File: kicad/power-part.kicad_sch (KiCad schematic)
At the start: 53 parts, among them Q10 BSS84, Q11 BSS123N, Q12 ZXMP10A17GTA, Q2 IPT012N08N5, Q3 IPT012N08N5, Q4 IPT012N08N5, Q5 IPT012N08N5, Q6 IPT012N08N5, Q7 IPT012N08N5, Q8 IPT012N08N5, Q9 IPT012N08N5

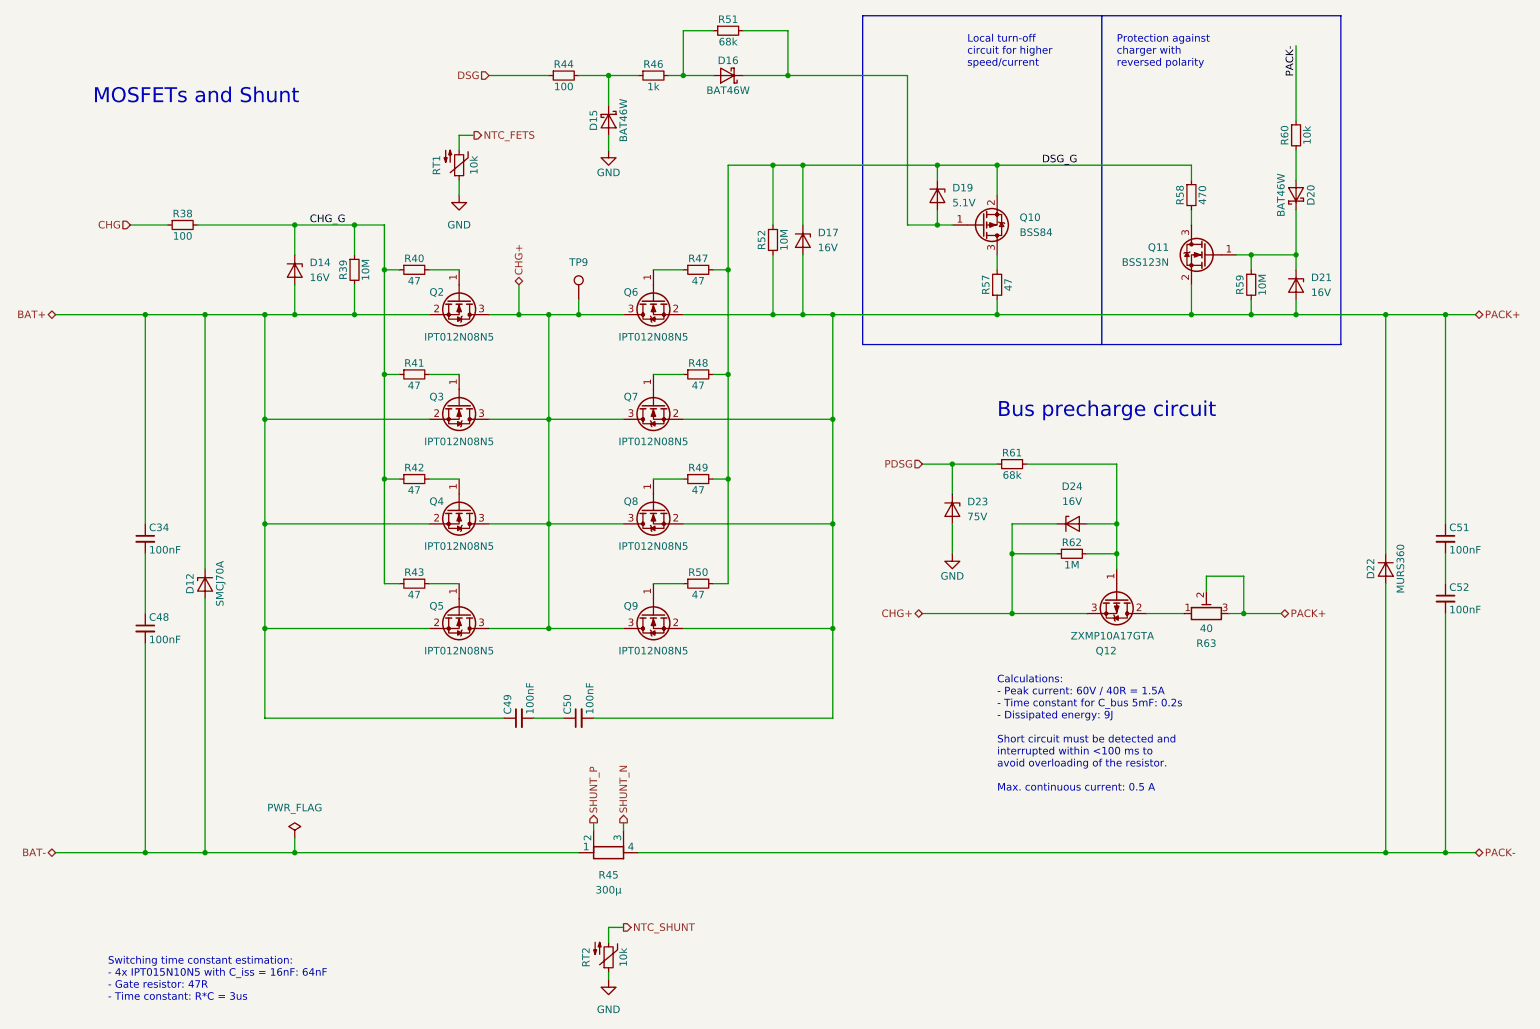
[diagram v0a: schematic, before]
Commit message: Create cost-optimized Lite variant of the BMS C1 v0.4.1
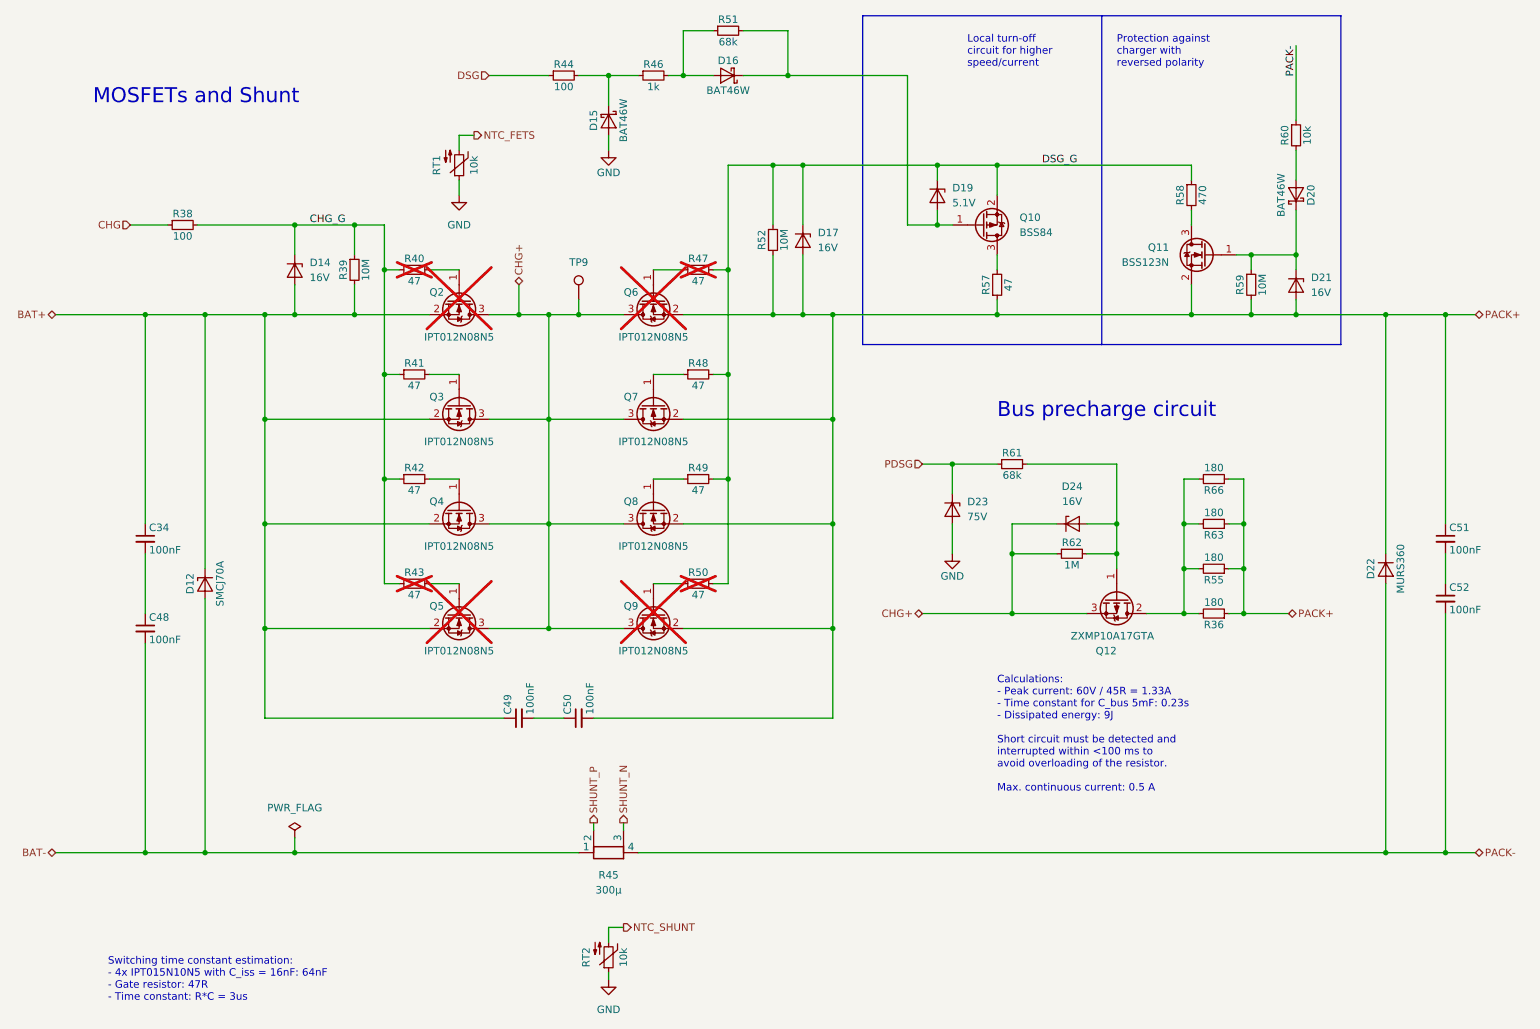
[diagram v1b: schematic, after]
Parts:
- removed R63: 40, LibreSolar:Bourns_PWR163, symbol Device:R_Potentiometer_Trim
- added R36, R55, R63, R66: 180, Resistor_SMD:R_2512_6332Metric_Pad1.40x3.35mm_HandSolder, symbol LibreSolar:R
- Q2, Q5, Q6, Q9, R40, R43, R47, R50: now not fitted
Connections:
- net PACK+: now also R36.1, R55.1, R63.1, R66.1
- net at Q12.2 (D): now also R36.2, R55.2, R63.2, R66.2
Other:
- note added: "Calculations: - Peak current: 60V / 45R = 1.33A - Time constant for C_bus 5mF: 0.23s - Dissipated energy: 9J Short circuit must be detected and interrupted within <100 ms to avoid overloading of the resistor. Max. continuous current: 0.5 A"
- note removed: "Calculations: - Peak current: 60V / 40R = 1.5A - Time constant for C_bus 5mF: 0.2s - Dissipated energy: 9J Short circuit must be detected and interrupted within <100 ms to avoid overloading of the resistor. Max. continuous current: 0.5 A"
- title: Libre Solar BMS C1 -> Libre Solar BMS C1 lite
